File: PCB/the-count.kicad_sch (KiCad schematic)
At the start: 5 parts, among them J4 PWR

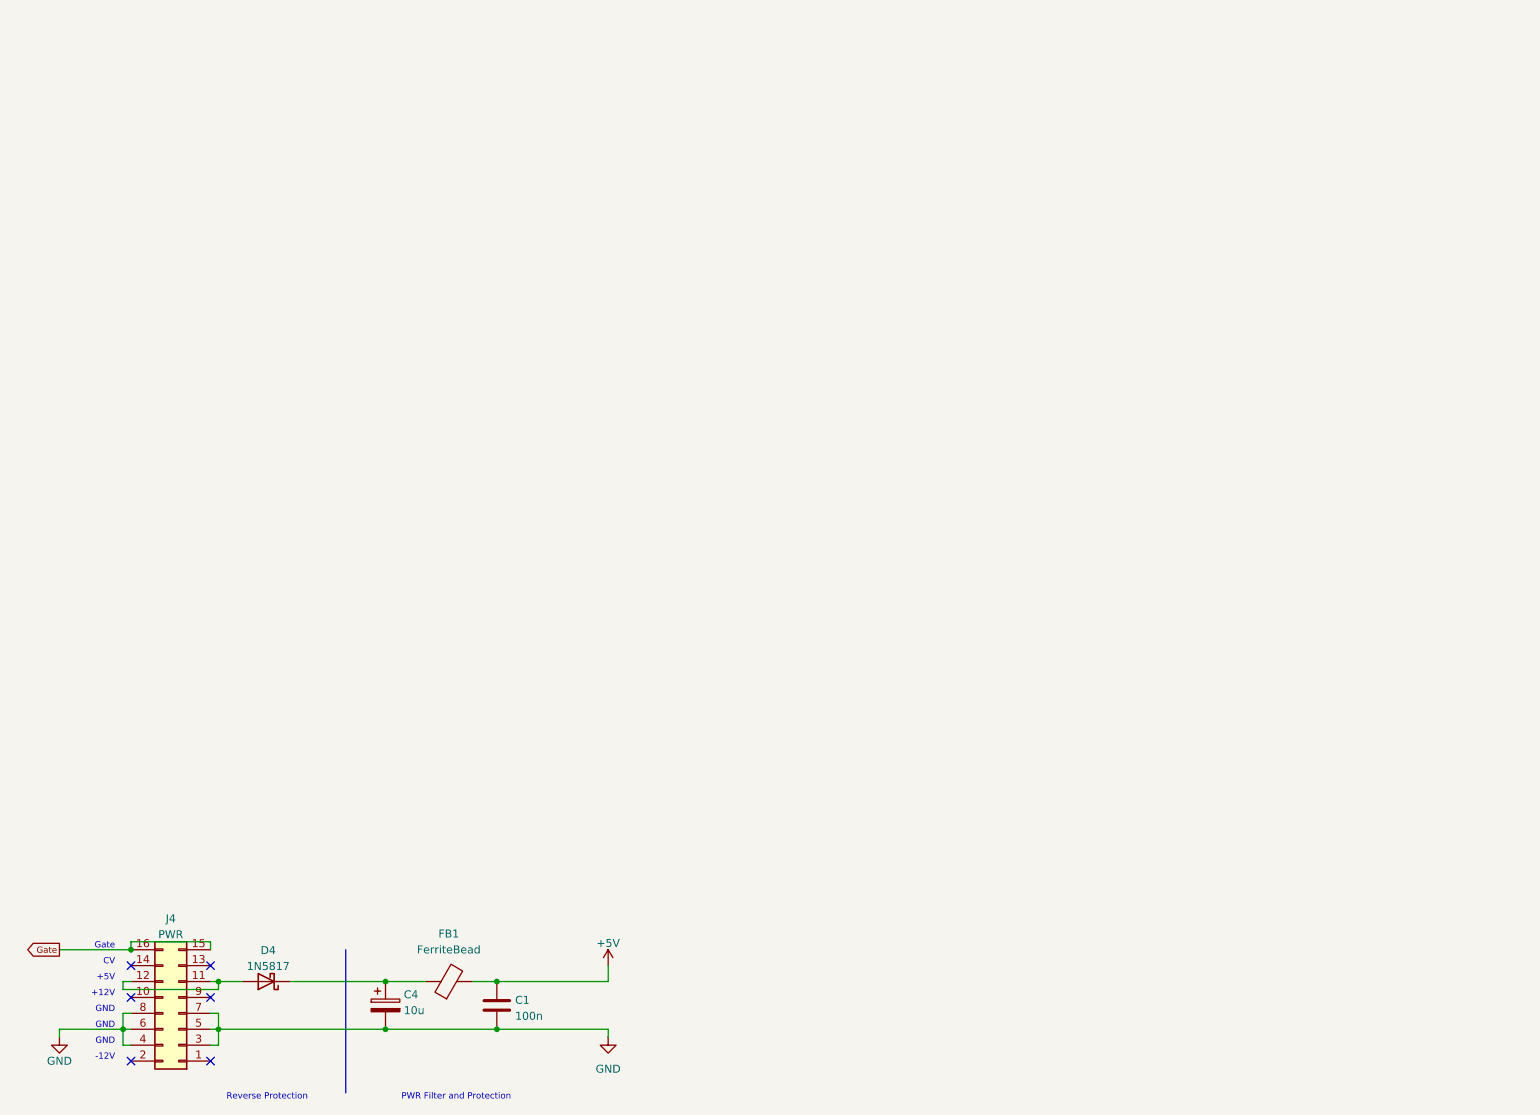
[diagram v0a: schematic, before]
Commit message: :sparkles: Add Gate output element
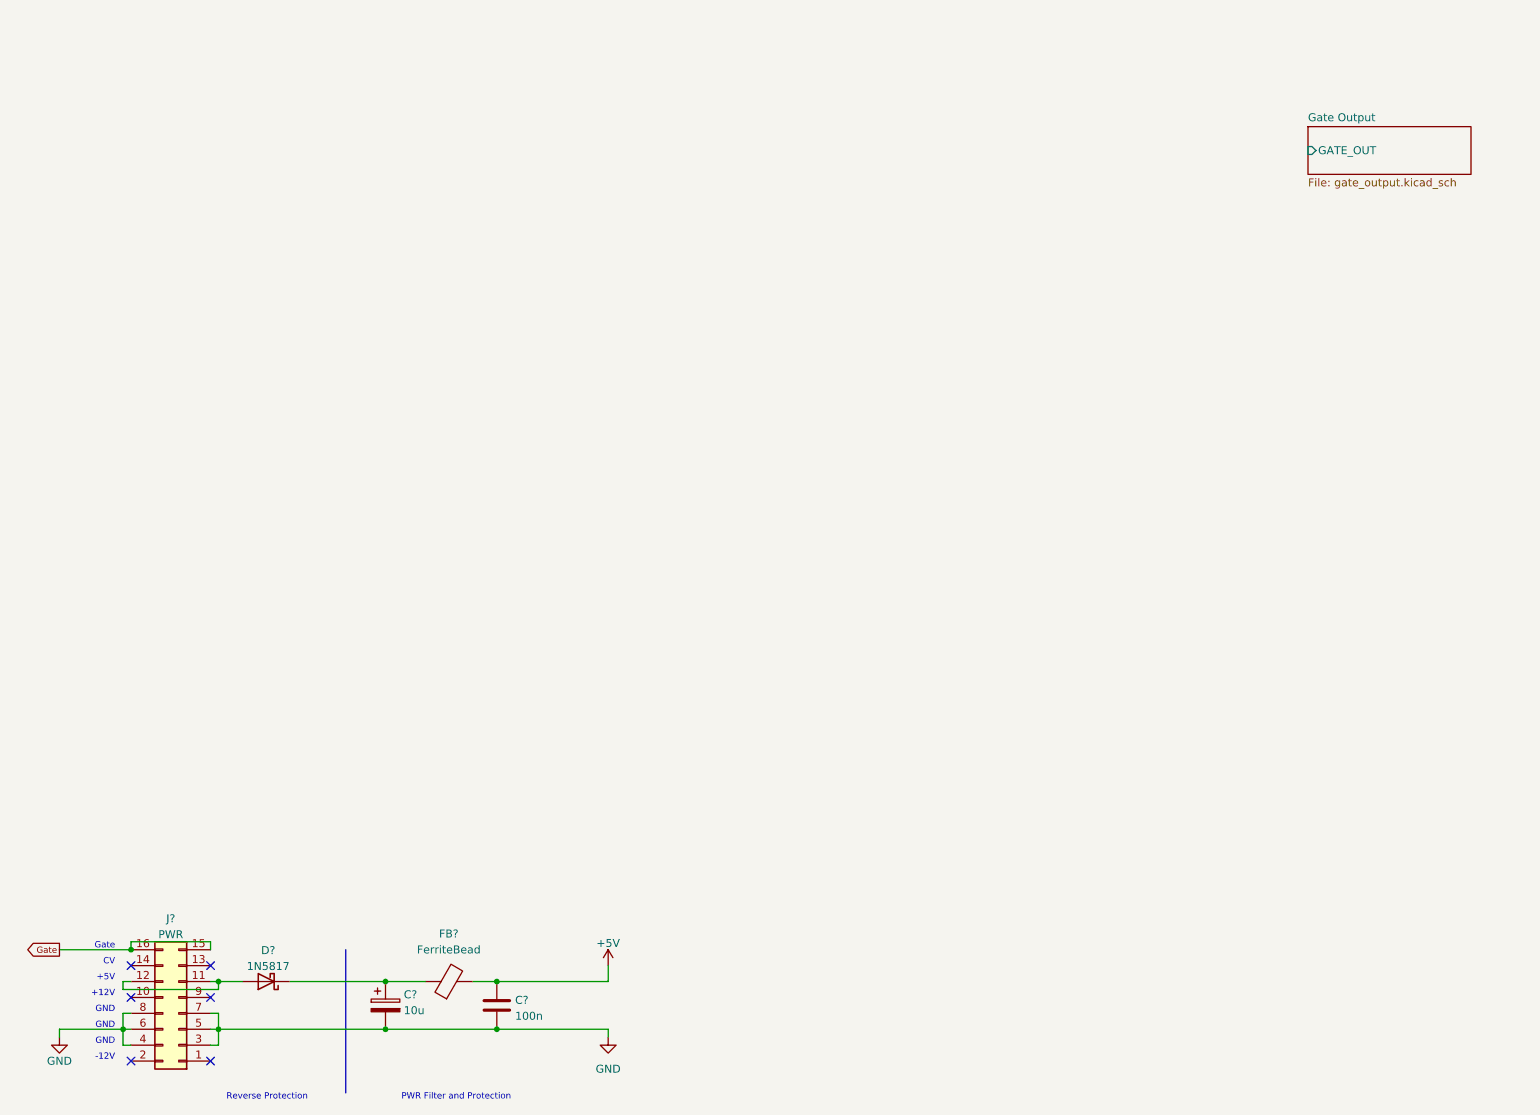
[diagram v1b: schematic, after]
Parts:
- renumbered C1 to C?, C4 to C?, D4 to D?, FB1 to FB?, J4 to J?
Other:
- added sheet Gate Output (gate_output.kicad_sch)
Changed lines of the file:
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@@
   (symbol (lib_id "Device:D_Schottky") (at 54.61 176.53 180) (unit 1)
     (in_bom yes) (on_board yes) (dnp no) (fields_autoplaced)
-    (property "Reference" "D4" (at 54.9275 171.5602 0)
+    (property "Reference" "D?" (at 54.9275 171.5602 0)
       (effects (font (size 1.27 1.27)))
     )
@@
       (project "eurorack-power-breakout"
         (path "/18b717ae-c948-4f75-a5e6-e6afbe279fcf"
-          (reference "D4") (unit 1)
-        )
-      )
-      (project "the-count"
-        (path "/69636855-5bea-4b1f-bae0-d5724c7c5e69"
-          (reference "D1") (unit 1)
+          (reference "D?") (unit 1)
+        )
+      )
+      (project "the-count"
+        (path "/69636855-5bea-4b1f-bae0-d5724c7c5e69"
+          (reference "D?") (unit 1)
         )
       )
@@
   (symbol (lib_id "Device:FerriteBead") (at 83.82 176.53 90) (unit 1)
     (in_bom yes) (on_board yes) (dnp no)
-    (property "Reference" "FB1" (at 83.7692 168.91 90)
+    (property "Reference" "FB?" (at 83.7692 168.91 90)
       (effects (font (size 1.27 1.27)))
     )
@@
       (project "eurorack-power-breakout"
         (path "/18b717ae-c948-4f75-a5e6-e6afbe279fcf"
-          (reference "FB1") (unit 1)
-        )
-      )
-      (project "the-count"
-        (path "/69636855-5bea-4b1f-bae0-d5724c7c5e69"
-          (reference "FB1") (unit 1)
+          (reference "FB?") (unit 1)
+        )
+      )
+      (project "the-count"
+        (path "/69636855-5bea-4b1f-bae0-d5724c7c5e69"
+          (reference "FB?") (unit 1)
         )
       )
@@
   (symbol (lib_id "Connector_Generic:Conn_02x08_Odd_Even") (at 40.64 181.61 180) (unit 1)
     (in_bom yes) (on_board yes) (dnp no) (fields_autoplaced)
-    (property "Reference" "J4" (at 39.37 166.4802 0)
+    (property "Reference" "J?" (at 39.37 166.4802 0)
       (effects (font (size 1.27 1.27)))
     )
@@
       (project "eurorack-power-breakout"
         (path "/18b717ae-c948-4f75-a5e6-e6afbe279fcf"
-          (reference "J4") (unit 1)
-        )
-      )
-      (project "the-count"
-        (path "/69636855-5bea-4b1f-bae0-d5724c7c5e69"
-          (reference "J1") (unit 1)
+          (reference "J?") (unit 1)
+        )
+      )
+      (project "the-count"
+        (path "/69636855-5bea-4b1f-bae0-d5724c7c5e69"
+          (reference "J?") (unit 1)
         )
       )
@@
   (symbol (lib_id "Device:C") (at 91.44 180.34 0) (unit 1)
     (in_bom yes) (on_board yes) (dnp no) (fields_autoplaced)
-    (property "Reference" "C1" (at 94.361 179.5053 0)
+    (property "Reference" "C?" (at 94.361 179.5053 0)
       (effects (font (size 1.27 1.27)) (justify left))
     )
@@
       (project "eurorack-power-breakout"
         (path "/18b717ae-c948-4f75-a5e6-e6afbe279fcf"
-          (reference "C1") (unit 1)
-        )
-      )
-      (project "the-count"
-        (path "/69636855-5bea-4b1f-bae0-d5724c7c5e69"
-          (reference "C1") (unit 1)
+          (reference "C?") (unit 1)
+        )
+      )
+      (project "the-count"
+        (path "/69636855-5bea-4b1f-bae0-d5724c7c5e69"
+          (reference "C?") (unit 1)
         )
       )
@@
   (symbol (lib_id "Device:C_Polarized") (at 73.66 180.34 0) (unit 1)
     (in_bom yes) (on_board yes) (dnp no) (fields_autoplaced)
-    (property "Reference" "C4" (at 76.581 178.6163 0)
+    (property "Reference" "C?" (at 76.581 178.6163 0)
       (effects (font (size 1.27 1.27)) (justify left))
     )
@@
       (project "eurorack-power-breakout"
         (path "/18b717ae-c948-4f75-a5e6-e6afbe279fcf"
-          (reference "C4") (unit 1)
-        )
-      )
-      (project "the-count"
-        (path "/69636855-5bea-4b1f-bae0-d5724c7c5e69"
-          (reference "C4") (unit 1)
+          (reference "C?") (unit 1)
+        )
+      )
+      (project "the-count"
+        (path "/69636855-5bea-4b1f-bae0-d5724c7c5e69"
+          (reference "C?") (unit 1)
         )
       )
@@
   (symbol (lib_id "power:GND") (at 21.59 185.42 0) (unit 1)
     (in_bom yes) (on_board yes) (dnp no)
-    (property "Reference" "#PWR01" (at 21.59 191.77 0)
+    (property "Reference" "#PWR?" (at 21.59 191.77 0)
       (effects (font (size 1.27 1.27)) hide)
     )
@@
       (project "eurorack-power-breakout"
         (path "/18b717ae-c948-4f75-a5e6-e6afbe279fcf"
-          (reference "#PWR01") (unit 1)
-        )
-      )
-      (project "the-count"
-        (path "/69636855-5bea-4b1f-bae0-d5724c7c5e69"
-          (reference "#PWR01") (unit 1)
+          (reference "#PWR?") (unit 1)
+        )
+      )
+      (project "the-count"
+        (path "/69636855-5bea-4b1f-bae0-d5724c7c5e69"
+          (reference "#PWR?") (unit 1)
         )
       )
@@
   (symbol (lib_id "power:+5V") (at 109.22 173.99 0) (unit 1)
     (in_bom yes) (on_board yes) (dnp no) (fields_autoplaced)
-    (property "Reference" "#PWR02" (at 109.22 177.8 0)
+    (property "Reference" "#PWR?" (at 109.22 177.8 0)
       (effects (font (size 1.27 1.27)) hide)
     )
@@
       (project "eurorack-power-breakout"
         (path "/18b717ae-c948-4f75-a5e6-e6afbe279fcf"
-          (reference "#PWR02") (unit 1)
-        )
-      )
-      (project "the-count"
-        (path "/69636855-5bea-4b1f-bae0-d5724c7c5e69"
-          (reference "#PWR02") (unit 1)
+          (reference "#PWR?") (unit 1)
+        )
+      )
+      (project "the-count"
+        (path "/69636855-5bea-4b1f-bae0-d5724c7c5e69"
+          (reference "#PWR?") (unit 1)
         )
       )
@@
   (symbol (lib_name "GND_1") (lib_id "power:GND") (at 109.22 185.42 0) (unit 1)
     (in_bom yes) (on_board yes) (dnp no) (fields_autoplaced)
-    (property "Reference" "#PWR04" (at 109.22 191.77 0)
+    (property "Reference" "#PWR?" (at 109.22 191.77 0)
       (effects (font (size 1.27 1.27)) hide)
     )
@@
       (project "the-count"
         (path "/69636855-5bea-4b1f-bae0-d5724c7c5e69"
-          (reference "#PWR04") (unit 1)
-        )
-      )
-    )
+          (reference "#PWR?") (unit 1)
+        )
+      )
+    )
+  )
+  (sheet (at 220.98 40.005) (size 26.035 7.62) (fields_autoplaced)
+    (stroke (width 0.1524) (type solid))
+    (fill (color 0 0 0 0.0000))
+    (property "Sheetname" "Gate Output" (at 220.98 39.2934 0)
+      (effects (font (size 1.27 1.27)) (justify left bottom))
+    )
+    (property "Sheetfile" "gate_output.kicad_sch" (at 220.98 48.2096 0)
+      (effects (font (size 1.27 1.27)) (justify left top))
+    )
+    (pin "GATE_OUT" input (at 220.98 43.815 180)
+      (effects (font (size 1.27 1.27)) (justify left))
+    )
+    (instances
+      (project "the-count"
+        (path "/69636855-5bea-4b1f-bae0-d5724c7c5e69" (page "2"))
+      )
+    )

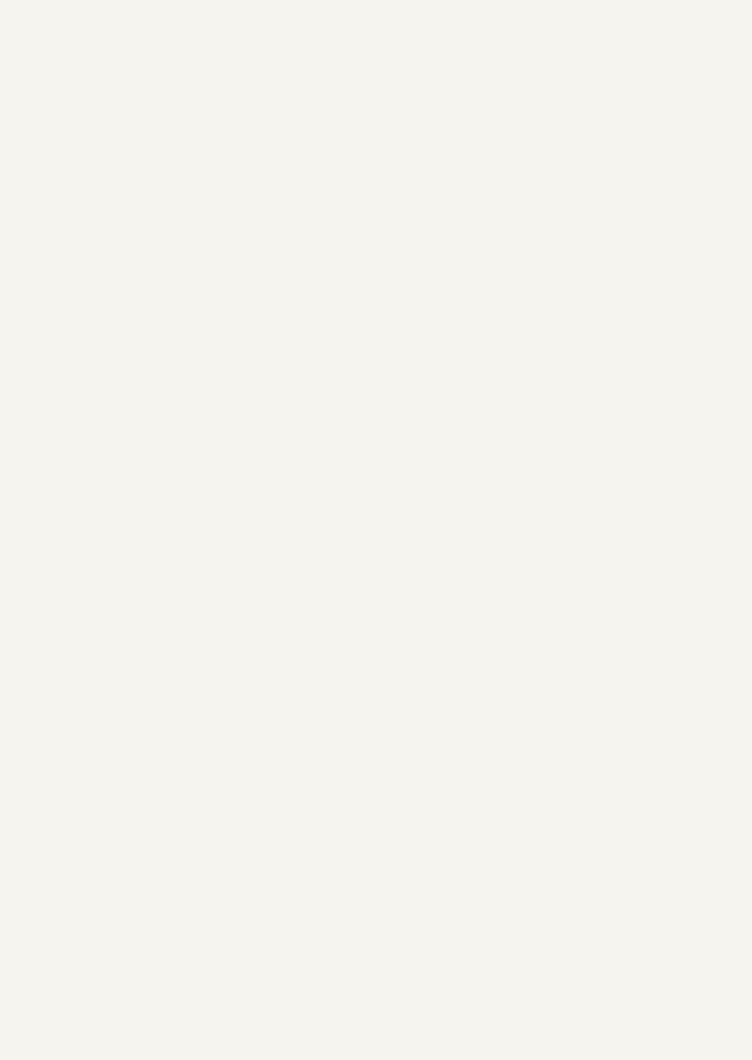
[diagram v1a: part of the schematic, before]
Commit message: :sparkles: Add count and reset input
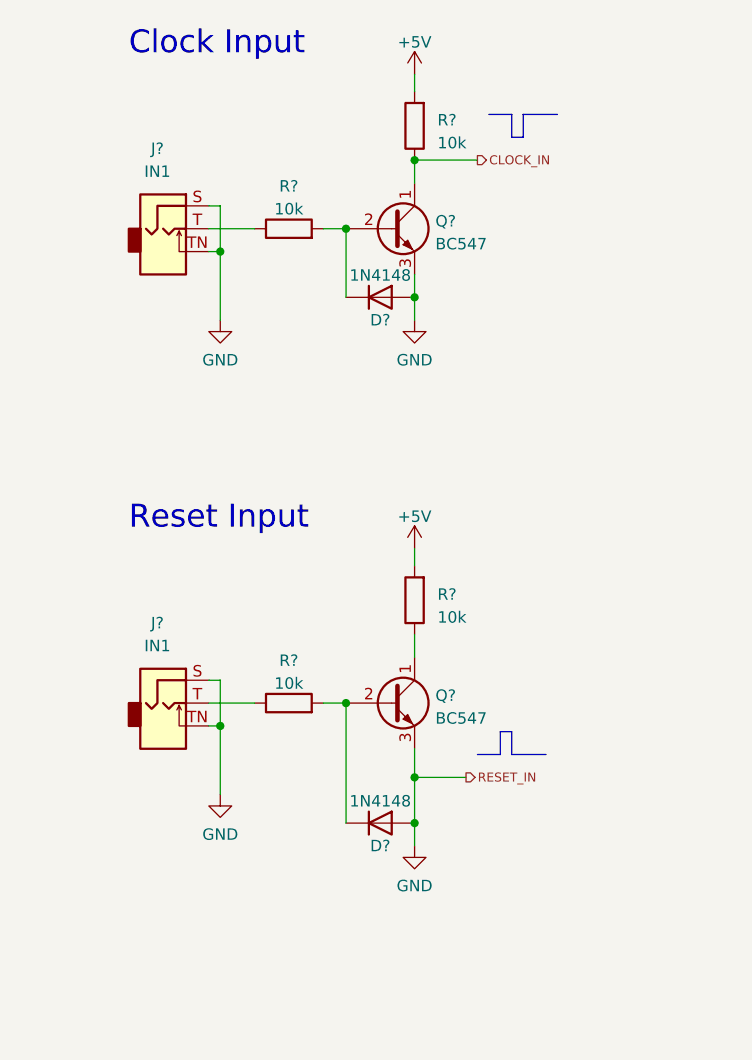
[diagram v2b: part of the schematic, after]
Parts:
- added D? (x2): 1N4148, Diode_THT:D_DO-35_SOD27_P7.62mm_Horizontal, symbol Diode:1N4148
- added J? (x2): IN1, moPsy:Jack_3.5mm_QingPu_WQP-PJ398SM_Vertical_CircularHoles_Centered, symbol Connector:AudioJack2_Ground_SwitchT
- added Q? (x2): BC547, Package_TO_SOT_THT:TO-92_Inline, symbol Transistor_BJT:BC547
- added R? (x4): 10k, Resistor_THT:R_Axial_DIN0207_L6.3mm_D2.5mm_P7.62mm_Horizontal, symbol Device:R
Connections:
- net +5V: now also R?.2, R?.2
- net GND: now also D?.2 (A), D?.2 (A), J?.S, J?.S, J?.TN, J?.TN, Q?.3 (E), Q?.3 (E)
- new net: Q?.1 (C), R?.1
- new net: D?.1 (K), Q?.2 (B), R?.2 (x2)
- new net: J?.T, R?.1 (x2)
- new net CLOCK_IN: Q?.1 (C), R?.1
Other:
- note added: "Clock Input"
- note added: "Reset Input"

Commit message: :sparkles: Add the counter logic
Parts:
- added C?: 100n, Capacitor_THT:C_Disc_D4.3mm_W1.9mm_P5.00mm, symbol Device:C
- added D? (x2): rt, LED_THT:LED_D3.0mm, symbol Device:LED
- added R? (x2): 1k, Resistor_THT:R_Axial_DIN0207_L6.3mm_D2.5mm_P7.62mm_Horizontal, symbol Device:R
- added U?: 4024, Package_DIP:DIP-14_W7.62mm_Socket_LongPads, symbol 4xxx_IEEE:4024
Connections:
- net +5V: now also C?.1, D?.2 (A), U?.14 (VDD)
- net CLOCK_IN: now also R?.1, U?.1 (~{CLK})
- net GND: now also C?.2, D?.2 (A), R?.1, U?.2 (MR), U?.7 (VSS)
- net Gate Output 2/GATE_OUT: now also U?.12 (Q0)
- new net: D?.1 (K), R?.2 (x2)
- new net Gate Output 16/GATE_OUT: U?.6 (Q3)
- new net Gate Output 32/GATE_OUT: U?.5 (Q4)
- new net Gate Output 4/GATE_OUT: U?.11 (Q1)
- new net Gate Output 64/GATE_OUT: U?.4 (Q5)
- new net Gate Output 8/GATE_OUT: U?.9 (Q2)
- no-connect marks 6 -> 7
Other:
- sheet Gate Output renamed Gate Output 2
- added sheet Gate Output 16 (gate_output.kicad_sch)
- added sheet Gate Output 32 (gate_output.kicad_sch)
- added sheet Gate Output 4 (gate_output.kicad_sch)
- added sheet Gate Output 64 (gate_output.kicad_sch)
- added sheet Gate Output 8 (gate_output.kicad_sch)

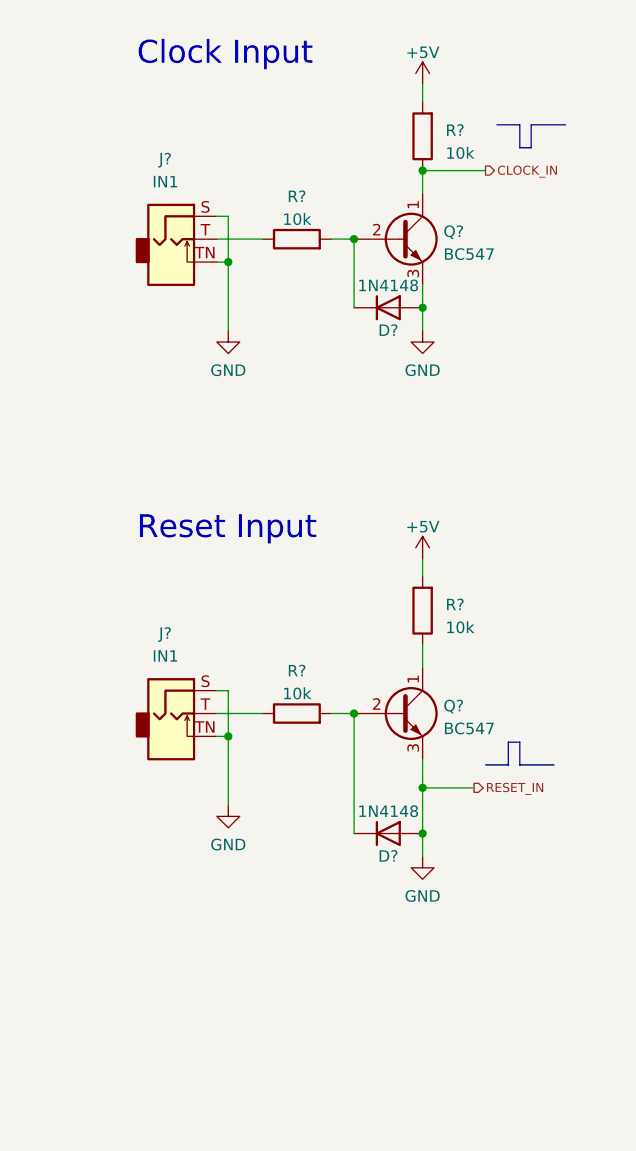
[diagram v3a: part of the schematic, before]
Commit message: :sparkles: Add bus gate reset option
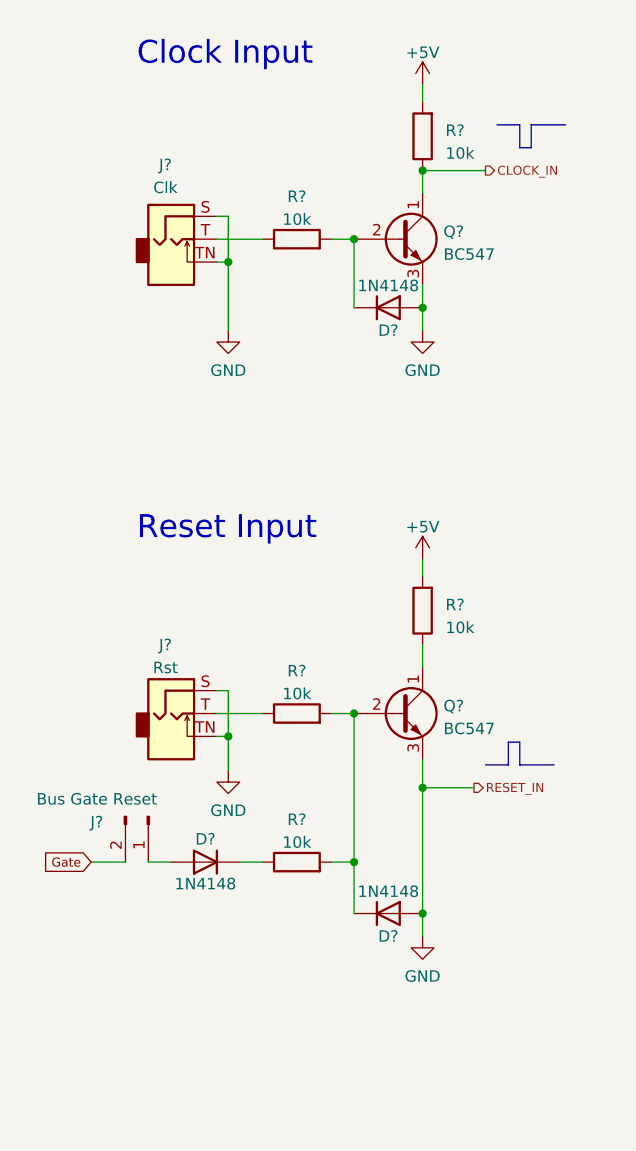
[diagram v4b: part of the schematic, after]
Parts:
- added D?: 1N4148, Diode_THT:D_DO-35_SOD27_P7.62mm_Horizontal, symbol Diode:1N4148
- added J?: Bus Gate Reset, Connector_PinHeader_2.54mm:PinHeader_1x02_P2.54mm_Vertical, symbol Connector:Conn_01x02_Pin
- added R?: 10k, Resistor_THT:R_Axial_DIN0207_L6.3mm_D2.5mm_P7.62mm_Horizontal, symbol Device:R
- J?: value IN1 -> Clk
- J?: value IN1 -> Rst
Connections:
- net Gate: now also J?.2 (Pin_2)
- net at D?.1 (K), Q?.2 (B), R?.2: now also R?.2
- new net: D?.1 (K), R?.1
- new net: D?.2 (A), J?.1 (Pin_1)
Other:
- moved on the sheet: D?
